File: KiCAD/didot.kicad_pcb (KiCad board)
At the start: 2 copper layers, 156.2 x 118.1 mm, 78 parts, among them J1 JST_BATTERY, J2 Display Socket, U1 nice!nano

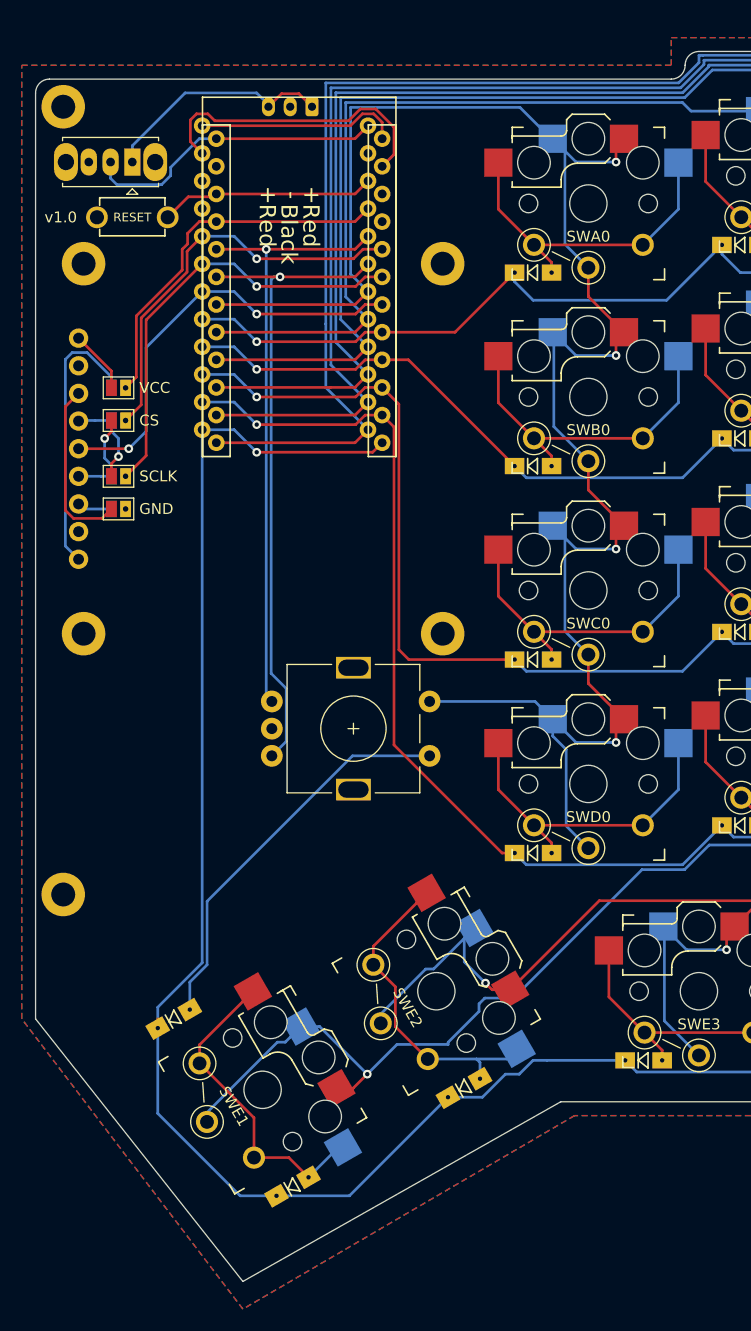
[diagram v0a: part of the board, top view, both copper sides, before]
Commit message: Move display to align with corner screw
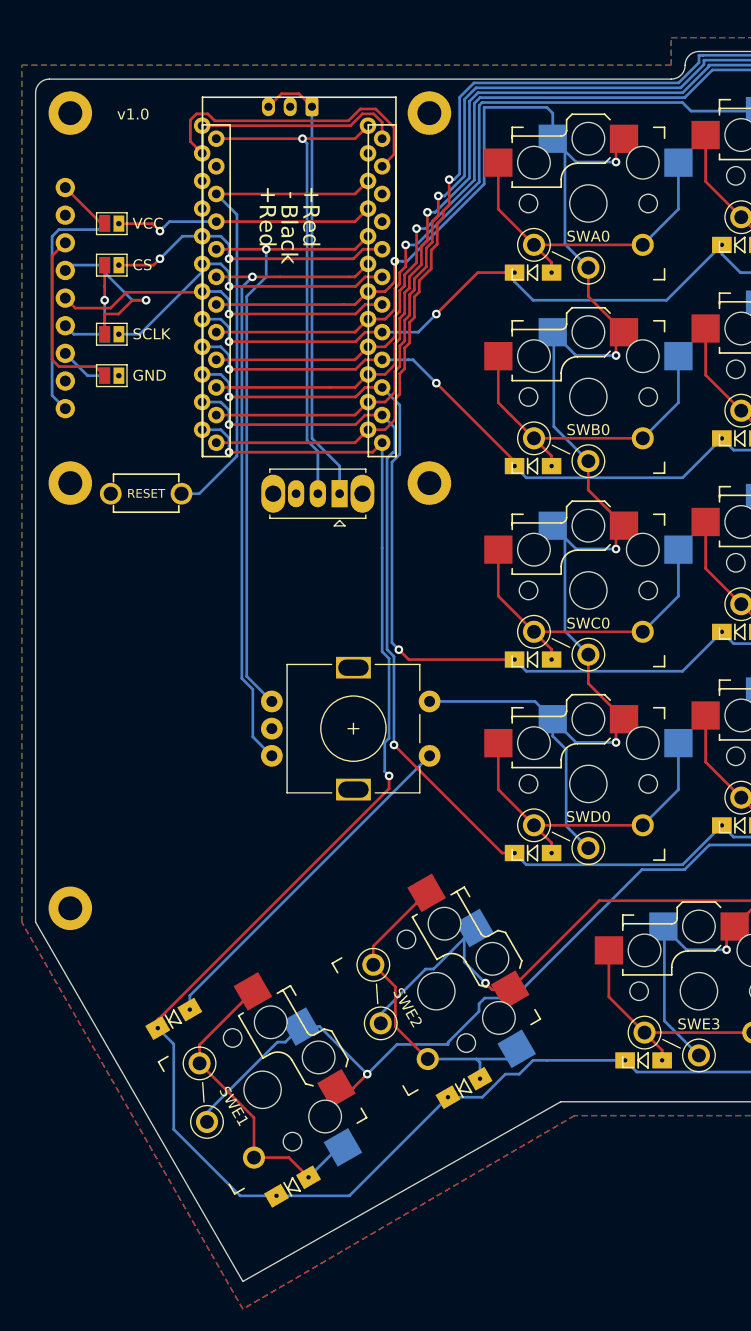
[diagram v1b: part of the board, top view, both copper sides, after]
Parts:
- removed the TH1 at (61.6, 78.9)
- removed the TH1 at (94.6, 78.9)
- removed the TH1 at (94.6, 44.9)
- removed the TH1 at (61.6, 44.9)
- removed the TH1 at (59.7, 30.5)
- added TH1: HOLE, Didot:M2_HOLE_PCB, F.Cu at (60.3, 31.1)
- added TH1: HOLE, Didot:M2_HOLE_PCB, F.Cu at (93.3, 31.1)
- added TH1: HOLE, Didot:M2_HOLE_PCB, F.Cu at (93.3, 65.1)
- added TH1: HOLE, Didot:M2_HOLE_PCB, F.Cu at (60.3, 65.1)
- moved SW_PWR1 35.9 mm to (85.1, 66.0)
- moved SW_RESET1 25.4 mm to (67.3, 66.0)
- moved JP1 15.1 mm to (64.2, 41.2)
- moved JP2 14.3 mm to (64.2, 45.0)
- moved J2 13.9 mm to (59.9, 48.1)
- moved JP3 13.1 mm to (64.2, 51.4)
- moved JP4 12.3 mm to (64.2, 55.2)
- moved TH1 1.43 mm to (60.3, 104.1)
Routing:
- net RESET: track 19.9 -> 46.4 mm
- net Net-(J1-Pad1): track 21.7 -> 41.8 mm
- net VCC: track 28.1 -> 47.6 mm, vias 0 -> 1
- net SCLK: track 40.2 -> 29.4 mm
- net col5: track 367.2 -> 357.3 mm, vias 5 -> 6
- net CS: track 37.6 -> 27.9 mm, vias 1 -> 2
- net VCOM: track 34.3 -> 24.7 mm, vias 0 -> 1
- net col4: track 342.6 -> 333.2 mm, vias 5 -> 6
- net col3: track 312.3 -> 303.6 mm, vias 5 -> 6
- net col2: track 288.4 -> 280.3 mm, vias 5 -> 6
- net col1: track 260.4 -> 252.9 mm, vias 6 -> 7
- net rowE: track 178.5 -> 185.7 mm, vias 1 -> 2
- net MOSI: track 39.2 -> 32.1 mm, vias 2 -> 1
- net Net-(J2-Pad4): track 9.17 -> 15.6 mm
- net col0: track 175.0 -> 169.6 mm, vias 4 -> 5
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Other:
- outline, holes or cut-outs redrawn

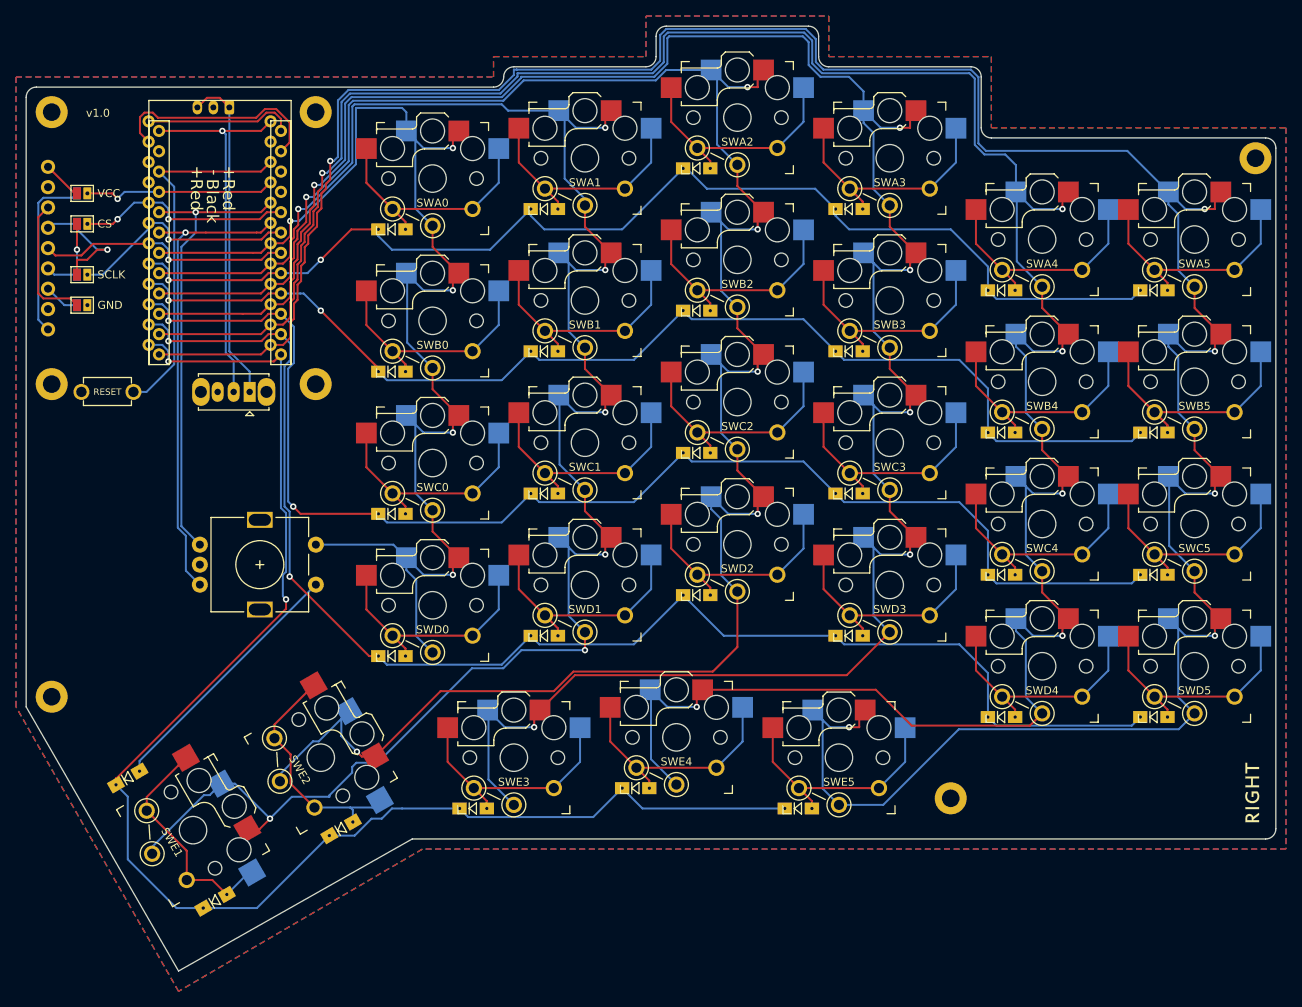
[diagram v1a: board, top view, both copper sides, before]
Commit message: Fix small ground pour issues
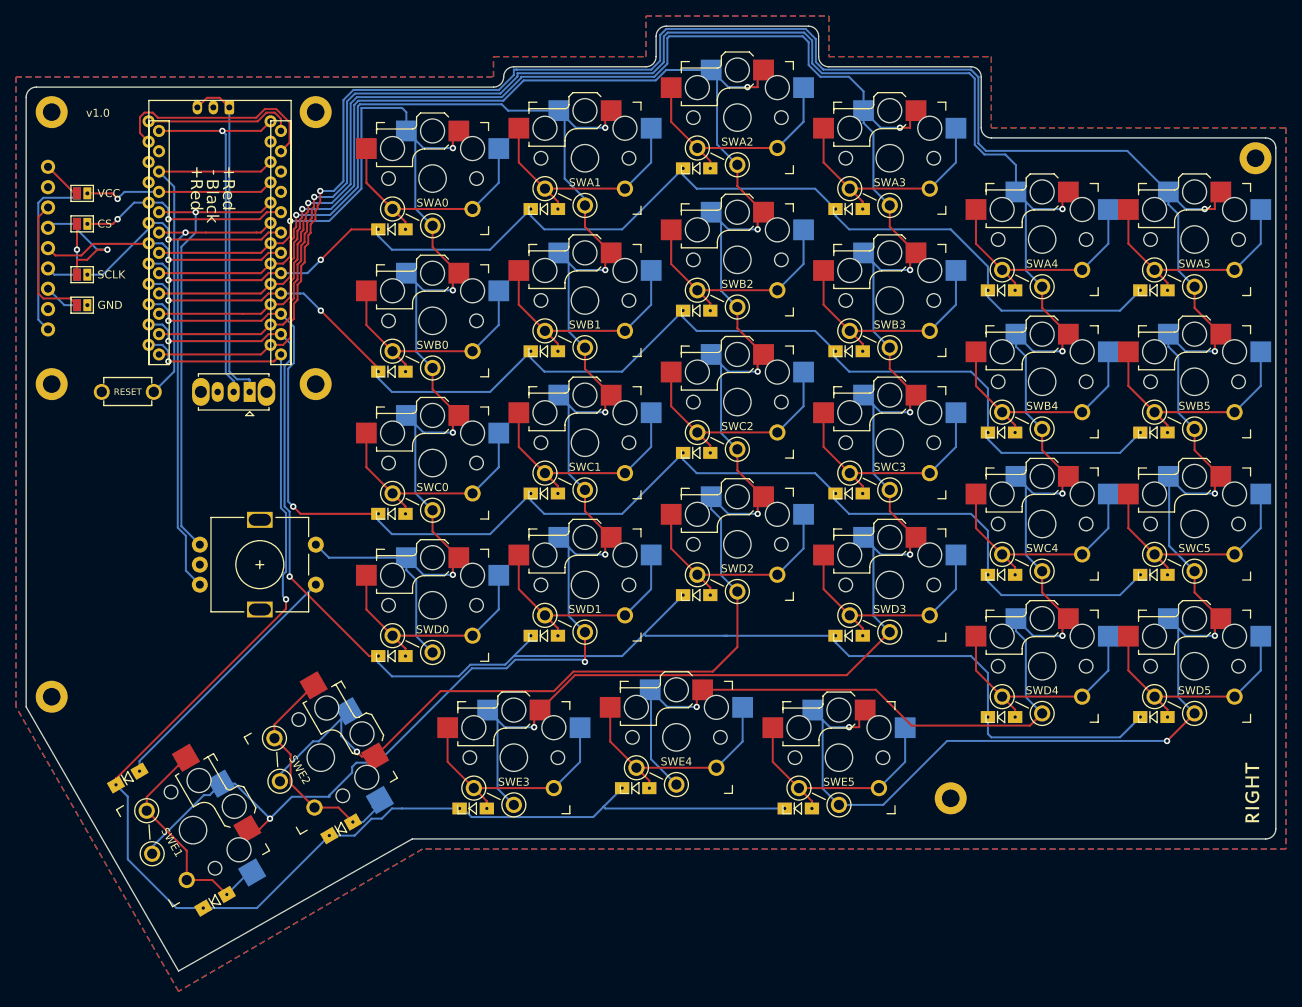
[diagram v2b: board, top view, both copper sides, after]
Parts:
- moved SW_RESET1 2.54 mm to (69.8, 66.0)
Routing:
- net rowD: track 175.8 -> 186.7 mm
- net rowC: track 166.2 -> 172.4 mm
- net rowB: track 145.6 -> 151.7 mm
- net col1: track 252.9 -> 255.6 mm
- net rowA: track 146.8 -> 149.5 mm
- net RESET: track 46.4 -> 44.3 mm
- net Net-(J1-Pad1): track 41.8 -> 43.8 mm
- net col0: track 169.6 -> 171.5 mm
- net rowE: track 185.7 -> 187.1 mm
- net Net-(DE2-Pad2): track 31.9 -> 33.1 mm
- net col2: track 280.3 -> 281.5 mm
- net col3: track 303.6 -> 304.6 mm
- net col4: track 333.2 -> 334.0 mm
- net col5: track 357.3 -> 357.6 mm, vias 6 -> 7
